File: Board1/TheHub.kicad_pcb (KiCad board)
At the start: 2 copper layers, 195.6 x 195.6 mm, 69 parts, among them J1 ARM_ADC_1, J10 SCIENCE + WHEELS POWER CONN, J11 RFD900, J12 I2C_1 Test Point, J13 I2C_2 Test Point, J14 ARDUINO NANO LEFT, J15 GPIO Test, J16 I2C_3 Test Point, J17 12V OUT, J18 7.4V IN, J19 ANALOG SENSORS, J2 ARM_ADC_2, J20 GPS, J21 COMPASS, J22 ARDUINO NANO RIGHT, J23 NucleoRight, J3 ARM_PWM_OUT, J4 ARM POWER CONN, J5 NucleoLeft, J6 SCI_ADC_1, J7 SCIENCE_PWM_OUT, J8 12V MAIN POWER, J9 WHEEL_ADC_1, U1 PRE-PCA9685, U2 PRE-ADS1115, U3 PRE-ADS1115, U4 PRE-PCA9685, U5 PRE-ADS1115, U6 TL1963, U7 LM340MP-5.0, U9 PRE-ADS1115

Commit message: Initialize the PCB
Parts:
- removed D7: LED, LEDs:LED_0805
- removed G*** (x2): LOGO, Board1:Logo1
- removed J1: ARM_ADC_1, Pin_Headers:Pin_Header_Straight_2x04_Pitch2.54mm
- removed J10: SCIENCE + WHEELS POWER CONN, Pin_Headers:Pin_Header_Straight_2x16_Pitch2.54mm
- removed J14: ARDUINO NANO LEFT, Socket_Strips:Socket_Strip_Straight_1x15_Pitch2.54mm
- removed J18: 7.4V IN, FoxWestern:XT60
- removed J19: ANALOG SENSORS, Pin_Headers:Pin_Header_Straight_2x05_Pitch2.54mm
- removed J2: ARM_ADC_2, Pin_Headers:Pin_Header_Straight_2x04_Pitch2.54mm
- removed J20: GPS, Socket_Strips:Socket_Strip_Straight_1x09_Pitch2.54mm
- removed J21: COMPASS, Socket_Strips:Socket_Strip_Straight_1x06_Pitch2.54mm
- removed J22: ARDUINO NANO RIGHT, Socket_Strips:Socket_Strip_Straight_1x15_Pitch2.54mm
- removed J3: ARM_PWM_OUT, Pin_Headers:Pin_Header_Straight_1x16_Pitch2.54mm
- removed J4: ARM POWER CONN, Pin_Headers:Pin_Header_Straight_2x16_Pitch2.54mm
- removed J6: SCI_ADC_1, Pin_Headers:Pin_Header_Straight_2x04_Pitch2.54mm
- removed J7: SCIENCE_PWM_OUT, Pin_Headers:Pin_Header_Straight_1x16_Pitch2.54mm
- removed J9: WHEEL_ADC_1, Pin_Headers:Pin_Header_Straight_2x04_Pitch2.54mm
- removed R13: 220, Resistors_SMD:R_0805
- removed the REF** at (131.4, 229.9)
- removed the REF** at (207.6, 230.5)
- removed the REF** at (65.4, 241.9)
- removed U1, U4: PRE-PCA9685, FoxWestern:PCA9685
- removed U2, U3, U5, U9: PRE-ADS1115, Socket_Strips:Socket_Strip_Straight_1x10_Pitch2.54mm
- added REF**: MountingHole_3.2mm_M3, Mounting_Holes:MountingHole_3.2mm_M3, F.Cu at (177.2, 92.1)
- added REF**: MountingHole_3.2mm_M3, Mounting_Holes:MountingHole_3.2mm_M3, F.Cu at (176.5, 55.2)
- added U10: ADXL377, FoxWestern:ADXL377, F.Cu at (108.0, 177.8)
- added U11: BNO055, FoxWestern:BNO055, F.Cu at (111.8, 208.3)
- added U12: MPL115A2, FoxWestern:MPL115A2, F.Cu at (77.5, 218.4)
- added U13: GPS, FoxWestern:Adafruit_GPS, F.Cu at (165.7, 199.4)
- added U8: MCP9808, FoxWestern:MCP9808, F.Cu at (77.5, 190.5)
- moved REF** 190.5 mm to (176.5, 228.0)
- moved REF** 187.9 mm to (66.7, 227.3)
- moved J8 150.4 mm to (158.8, 87.6), turned to 0 degrees
- moved J17 148.9 mm to (158.8, 97.2), turned to 0 degrees
- moved REF** 70.2 mm to (173.4, 185.4)
- moved J16 63.7 mm to (167.8, 173.5)
- moved R11 63.7 mm to (161.4, 173.5)
- moved R12 63.7 mm to (161.4, 169.7)
- moved J13 39.9 mm to (167.8, 162.7)
- moved R10 39.9 mm to (161.4, 158.9)
- moved R5 39.9 mm to (161.4, 162.7)
- moved R6 37.0 mm to (165.9, 129.0)
- moved J15 37.0 mm to (159.5, 130.3)
- moved R7 37.0 mm to (165.9, 132.8)
- moved R8 37.0 mm to (165.9, 136.7)
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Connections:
- net /A4 renamed /PB3
- net /A5 renamed /PB10
- J23 pad 33: /PA10 -> /GPS_FIX
- J5 pad 28: /PA0 -> /A0
- J5 pad 30: /PA1 -> /A1
- J5 pad 32: /PA4 -> /A2
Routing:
- net +3V3: track 645.6 -> 21.8 mm, vias 10 -> 0
- net /PB7: track 418.4 -> 5.72 mm, vias 3 -> 0
- net /PB6: track 354.4 -> 5.93 mm, vias 2 -> 0
- net +12V: track 311.7 -> 53.9 mm
- net /PB10: track 253.8 -> 5.93 mm, vias 5 -> 0
- net /7.4V: track 239.6 -> 0.00 mm
- net /PB3: track 227.3 -> 5.40 mm, vias 2 -> 0
- net /PA8: track 171.0 -> 5.93 mm, vias 1 -> 0
- net /PC9: track 132.2 -> 5.40 mm, vias 2 -> 0
- net /PC5: track 65.0 -> 25.5 mm, vias 1 -> 0
- net /PA6: track 69.1 -> 30.7 mm
- net /PA7: track 69.6 -> 31.2 mm
- net /PC4: track 92.3 -> 54.0 mm, vias 2 -> 1
- net GND: track 89.2 -> 70.1 mm, vias 6 -> 4
- net /TX1: track 13.3 -> 0.00 mm
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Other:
- board text added: "I2C_1"
- board text added: "I2C_2"
- board text added: "I2C_3"
- board text removed: "0X48"
- board text removed: "0X49"
- board text removed: "0X4A"
- board text removed: "0X4B"
- board text removed: "3V3"
- board text removed: "7.4V"
- board text removed: "A0"
- board text removed: "A1"
- board text removed: "A2"
- board text removed: "A3"
- board text removed: "ADS1115"
- board text removed: "ANALOG"
- board text removed: "CARD1"
- board text removed: "CARD2"
- board text removed: "COMPASS"
- board text removed: "GPS"
- board text removed: "NO USE"
- board text removed: "PCA9685"
- board text removed: "RX"
- board text removed: "Solder address pins"
- board text removed: "TX"

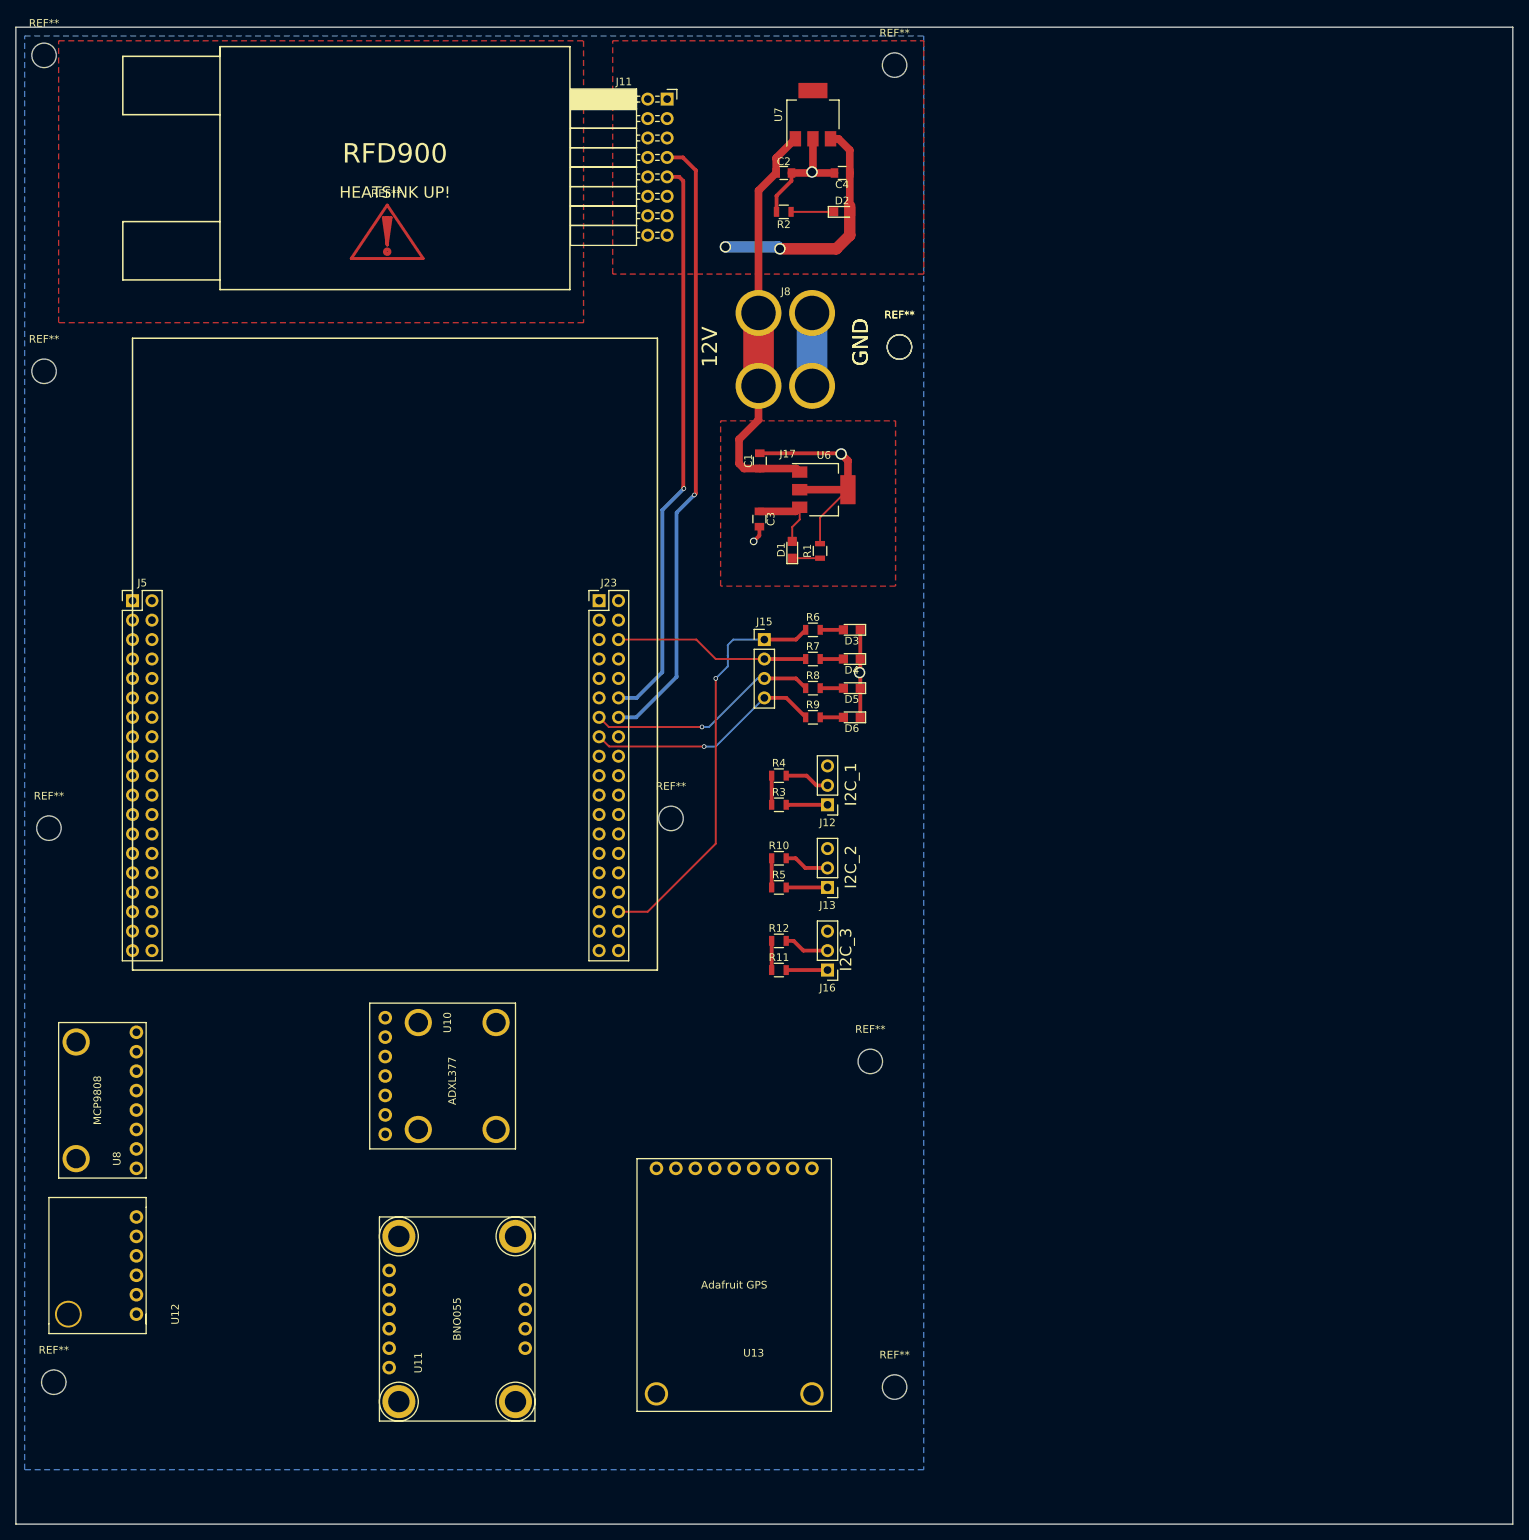
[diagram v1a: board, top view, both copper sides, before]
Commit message: Make PCB have smaller profile
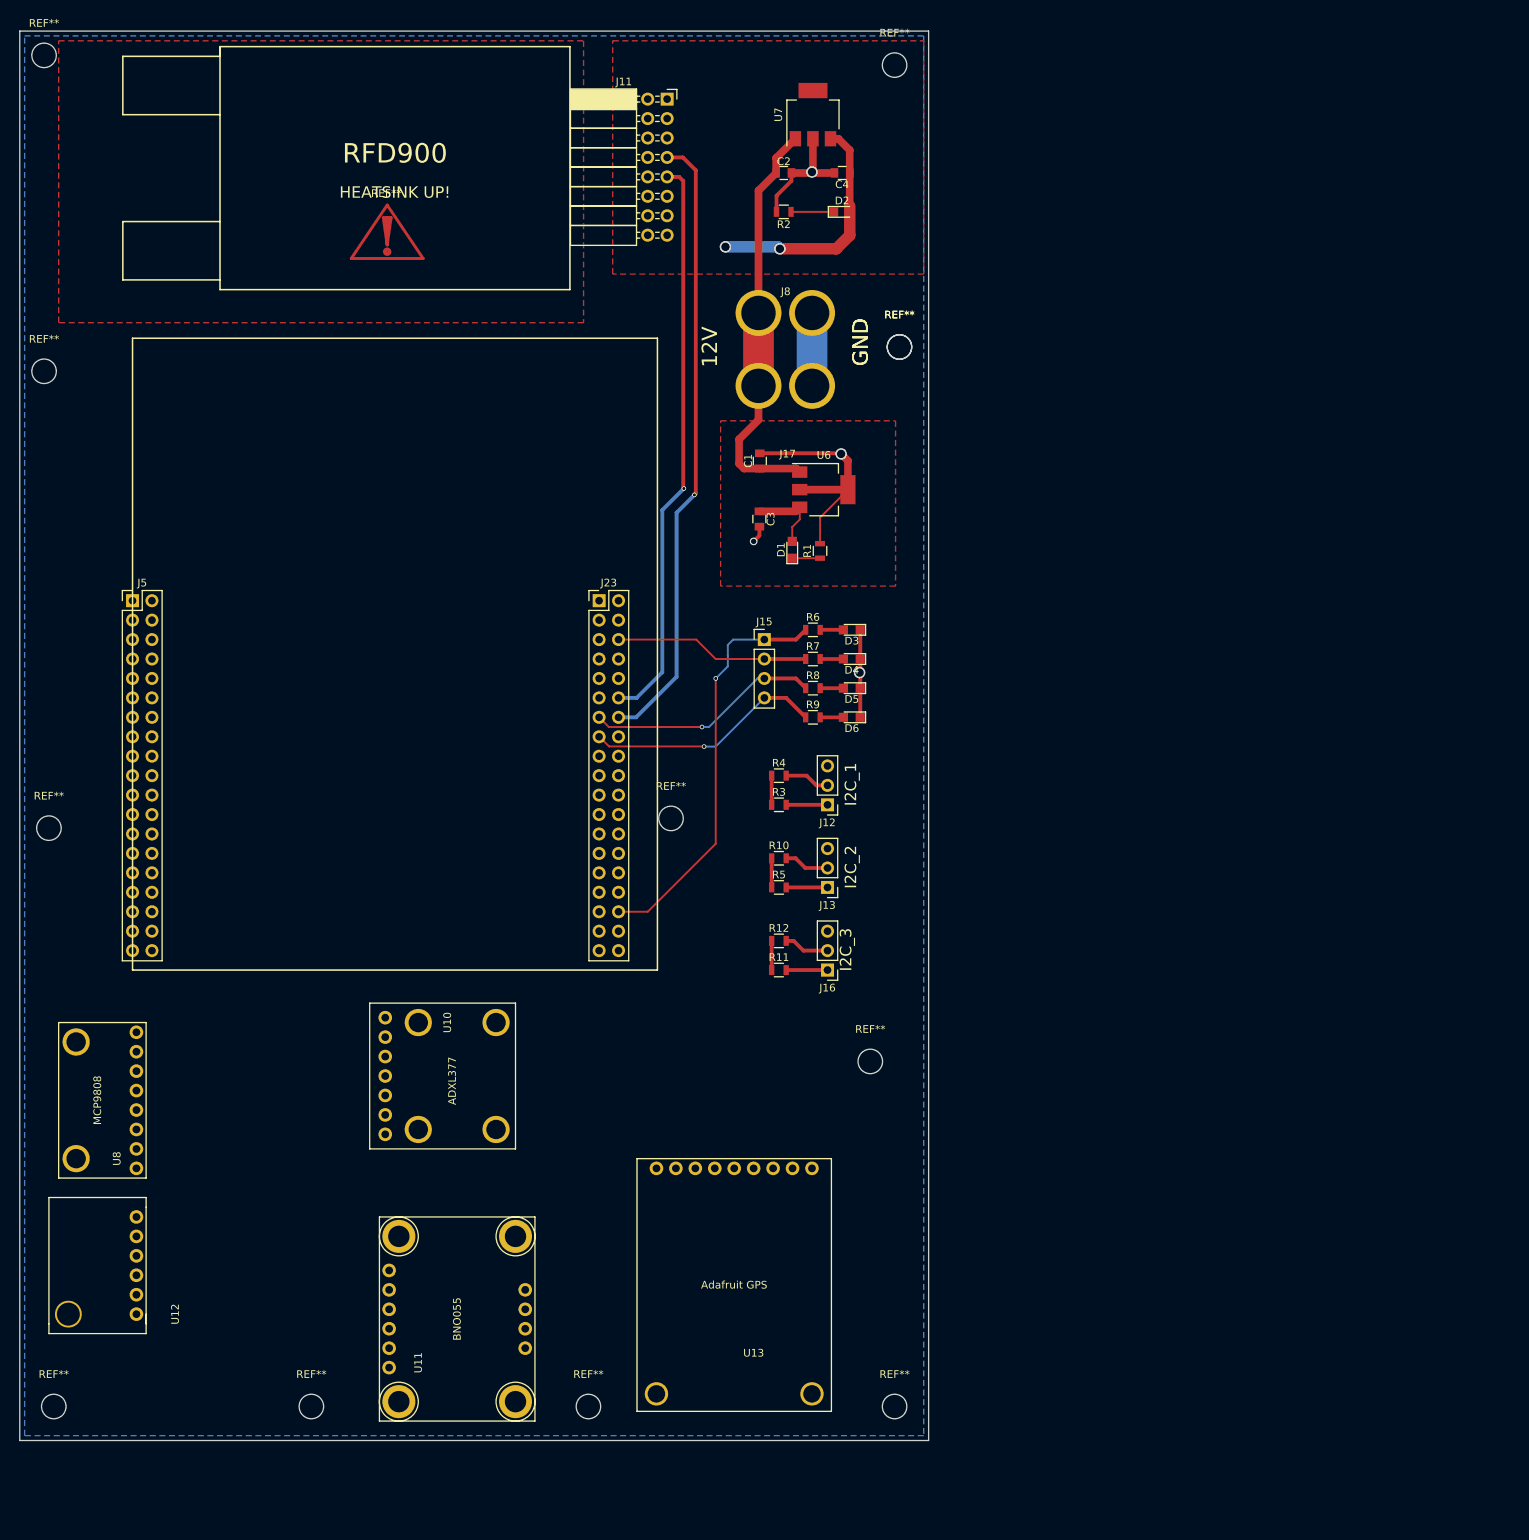
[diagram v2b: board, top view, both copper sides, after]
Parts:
- added REF**: MountingHole_3.2mm_M3, Mounting_Holes:MountingHole_3.2mm_M3, F.Cu at (100.3, 230.5)
- added REF**: MountingHole_3.2mm_M3, Mounting_Holes:MountingHole_3.2mm_M3, F.Cu at (136.5, 230.5)
- moved REF** 3.17 mm to (66.7, 230.5)
- moved REF** 2.54 mm to (176.5, 230.5)
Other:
- board size 195.6 x 195.6 mm -> 118.7 x 184.1 mm
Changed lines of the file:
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@@
     (tracks 135)
     (zones 0)
-    (modules 49)
+    (modules 51)
     (nets 107)
   )
@@
   )
   (module Mounting_Holes:MountingHole_3.2mm_M3 (layer F.Cu)
-    (at 66.675 227.33)
+    (at 66.675 230.505)
     (descr "Mounting Hole 3.2mm, no annular, M3")
     (tags "mounting hole 3.2mm no annular m3")
@@
   )
   (module Mounting_Holes:MountingHole_3.2mm_M3 (layer F.Cu)
-    (at 176.53 227.965)
+    (at 176.53 230.505)
     (descr "Mounting Hole 3.2mm, no annular, M3")
     (tags "mounting hole 3.2mm no annular m3")
@@
     (pad 1 np_thru_hole circle (at 0 0) (size 3.2 3.2) (drill 3.2) (layers *.Cu *.Mask))
   )
+  (module Mounting_Holes:MountingHole_3.2mm_M3 (layer F.Cu)
+    (at 100.33 230.505)
+    (descr "Mounting Hole 3.2mm, no annular, M3")
+    (tags "mounting hole 3.2mm no annular m3")
+    (attr virtual)
+    (fp_text reference REF** (at 0 -4.2) (layer F.SilkS)
+      (effects (font (size 1 1) (thickness 0.15)))
+    )
+    (fp_text value MountingHole_3.2mm_M3 (at 0 4.2) (layer F.Fab)
+      (effects (font (size 1 1) (thickness 0.15)))
+    )
+    (fp_text user %R (at 0.3 0) (layer F.Fab)
+      (effects (font (size 1 1) (thickness 0.15)))
+    )
+    (fp_circle (center 0 0) (end 3.2 0) (layer Cmts.User) (width 0.15))
+    (fp_circle (center 0 0) (end 3.45 0) (layer F.CrtYd) (width 0.05))
+    (pad 1 np_thru_hole circle (at 0 0) (size 3.2 3.2) (drill 3.2) (layers *.Cu *.Mask))
+  )
+  (module Mounting_Holes:MountingHole_3.2mm_M3 (layer F.Cu)
+    (at 136.525 230.505)
+    (descr "Mounting Hole 3.2mm, no annular, M3")
+    (tags "mounting hole 3.2mm no annular m3")
+    (attr virtual)
+    (fp_text reference REF** (at 0 -4.2) (layer F.SilkS)
+      (effects (font (size 1 1) (thickness 0.15)))
+    )
+    (fp_text value MountingHole_3.2mm_M3 (at 0 4.2) (layer F.Fab)
+      (effects (font (size 1 1) (thickness 0.15)))
+    )
+    (fp_text user %R (at 0.3 0) (layer F.Fab)
+      (effects (font (size 1 1) (thickness 0.15)))
+    )
+    (fp_circle (center 0 0) (end 3.2 0) (layer Cmts.User) (width 0.15))
+    (fp_circle (center 0 0) (end 3.45 0) (layer F.CrtYd) (width 0.05))
+    (pad 1 np_thru_hole circle (at 0 0) (size 3.2 3.2) (drill 3.2) (layers *.Cu *.Mask))
+  )
+  (gr_line (start 62.23 50.8) (end 62.23 234.95) (angle 90) (layer Edge.Cuts) (width 0.15))
+  (gr_line (start 180.975 234.95) (end 180.975 50.8) (angle 90) (layer Edge.Cuts) (width 0.15))
+  (gr_line (start 180.975 234.95) (end 62.23 234.95) (angle 90) (layer Edge.Cuts) (width 0.15))
+  (gr_line (start 62.23 50.8) (end 180.975 50.8) (angle 90) (layer Edge.Cuts) (width 0.15))
   (gr_text GND (at 172.085 91.44 90) (layer F.SilkS)
     (effects (font (size 2 2) (thickness 0.3)))
@@
     (effects (font (size 1.5 1.5) (thickness 0.3)))
   )
-  (gr_text "The Hub, Board Rev. 1\nTo Rapid Prototype\nDanny Mallek 6/9/2017" (at 118.745 238.125) (layer B.SilkS)
+  (gr_text "The Hub, Board Rev. 1\nTo Rapid Prototype\nDanny Mallek 6/9/2017" (at 83.82 229.87) (layer B.SilkS)
     (effects (font (size 1.5 1.5) (thickness 0.3)) (justify mirror))
   )
@@
   (gr_line (start 134.112 52.832) (end 88.392 52.832) (angle 90) (layer F.SilkS) (width 0.2))
   (gr_line (start 134.112 84.582) (end 134.112 52.832) (angle 90) (layer F.SilkS) (width 0.2))
-  (gr_line (start 61.722 245.872) (end 61.722 50.292) (angle 90) (layer Edge.Cuts) (width 0.15))
-  (gr_line (start 257.302 245.872) (end 61.722 245.872) (angle 90) (layer Edge.Cuts) (width 0.15))
-  (gr_line (start 257.302 50.292) (end 257.302 245.872) (angle 90) (layer Edge.Cuts) (width 0.15))
-  (gr_line (start 61.722 50.292) (end 257.302 50.292) (angle 90) (layer Edge.Cuts) (width 0.15))
   (segment (start 158.75 87.63) (end 158.75 71.644) (width 1) (layer F.Cu) (net 1))
   (segment (start 158.75 71.644) (end 161.052 69.342) (width 1) (layer F.Cu) (net 1))
@@
     (polygon
       (pts
-        (xy 180.34 238.76) (xy 62.865 238.76) (xy 62.865 51.435) (xy 180.34 51.435)
+        (xy 180.34 234.315) (xy 62.865 234.315) (xy 62.865 51.435) (xy 180.34 51.435)
       )
     )

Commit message: Created center line and aligned gyro and accelerometers
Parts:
- moved U13 2.92 mm to (168.7, 199.4)
- moved REF** 2.54 mm to (139.1, 230.4)
- moved U11 2.03 mm to (113.8, 208.3)
- moved U10 1.91 mm to (109.9, 177.8)
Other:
- board text added: "Center Line"
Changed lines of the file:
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@@
     (links 94)
     (no_connects 28)
-    (area 61.646999 50.216999 257.377001 245.947001)
+    (area 62.154999 50.724999 181.050001 235.025001)
     (thickness 1.6)
-    (drawings 31)
+    (drawings 33)
     (tracks 135)
     (zones 0)
@@
   )
   (module FoxWestern:ADXL377 (layer F.Cu)
-    (at 107.95 177.8 270)
+    (at 109.855 177.8 270)
     (fp_text reference U10 (at 2.54 -10.16 270) (layer F.SilkS)
       (effects (font (size 1 1) (thickness 0.15)))
@@
   )
   (module FoxWestern:BNO055 (layer F.Cu)
-    (at 111.76 208.28 270)
+    (at 113.792 208.28 270)
     (fp_text reference U11 (at 16.51 -2.54 270) (layer F.SilkS)
       (effects (font (size 1 1) (thickness 0.15)))
@@
   )
   (module FoxWestern:Adafruit_GPS (layer F.Cu)
-    (at 165.735 199.39 180)
+    (at 168.656 199.39 180)
     (fp_text reference U13 (at 7.62 -24.13 180) (layer F.SilkS)
       (effects (font (size 1 1) (thickness 0.15)))
@@
   )
   (module Mounting_Holes:MountingHole_3.2mm_M3 (layer F.Cu)
-    (at 136.525 230.505)
+    (at 139.065 230.378)
     (descr "Mounting Hole 3.2mm, no annular, M3")
     (tags "mounting hole 3.2mm no annular m3")
@@
     (pad 1 np_thru_hole circle (at 0 0) (size 3.2 3.2) (drill 3.2) (layers *.Cu *.Mask))
   )
+  (gr_text "Center Line" (at 120.904 200.914 90) (layer F.SilkS)
+    (effects (font (size 1.5 1.5) (thickness 0.3)))
+  )
+  (gr_line (start 121.666 235.204) (end 121.666 174.371) (angle 90) (layer F.SilkS) (width 0.2))
   (gr_line (start 62.23 50.8) (end 62.23 234.95) (angle 90) (layer Edge.Cuts) (width 0.15))
   (gr_line (start 180.975 234.95) (end 180.975 50.8) (angle 90) (layer Edge.Cuts) (width 0.15))
@@
     (effects (font (size 2 2) (thickness 0.3)))
   )
-  (gr_line (start 76.962 90.932) (end 145.542 90.932) (angle 90) (layer F.SilkS) (width 0.2))
-  (gr_line (start 145.542 173.482) (end 76.962 173.482) (angle 90) (layer F.SilkS) (width 0.2))
-  (gr_line (start 145.542 173.482) (end 145.542 90.932) (angle 90) (layer F.SilkS) (width 0.2))
-  (gr_line (start 76.962 173.482) (end 76.962 90.932) (angle 90) (layer F.SilkS) (width 0.2))
+  (gr_line (start 74.422 90.932) (end 143.002 90.932) (angle 90) (layer F.SilkS) (width 0.2))
+  (gr_line (start 143.002 173.482) (end 74.422 173.482) (angle 90) (layer F.SilkS) (width 0.2))
+  (gr_line (start 143.002 173.482) (end 143.002 90.932) (angle 90) (layer F.SilkS) (width 0.2))
+  (gr_line (start 74.422 173.482) (end 74.422 90.932) (angle 90) (layer F.SilkS) (width 0.2))
   (gr_text "HEATSINK UP!" (at 111.252 71.882) (layer F.SilkS)
     (effects (font (size 1.5 1.5) (thickness 0.3)))
